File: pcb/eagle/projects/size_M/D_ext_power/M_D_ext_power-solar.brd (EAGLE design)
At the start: 30 parts

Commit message: changed type of 3.3V converter back to LM3671
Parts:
- D.L1: value 4u7 -> 2u2
- D.U2: value MCP1603T-330I -> LM3671_3.3
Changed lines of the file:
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@@
 <grid distance="1" unitdist="mil" unit="mil" style="lines" multiple="1" display="yes" altdistance="0.1" altunitdist="mm" altunit="mm"/>
 <layers>
-<layer number="1" name="Top" color="4" fill="1" visible="no" active="yes"/>
-<layer number="16" name="Bottom" color="1" fill="1" visible="no" active="yes"/>
+<layer number="1" name="Top" color="4" fill="1" visible="yes" active="yes"/>
+<layer number="16" name="Bottom" color="1" fill="1" visible="yes" active="yes"/>
 <layer number="17" name="Pads" color="2" fill="1" visible="yes" active="yes"/>
 <layer number="18" name="Vias" color="2" fill="1" visible="yes" active="yes"/>
@@
 <layer number="20" name="Dimension" color="24" fill="1" visible="yes" active="yes"/>
 <layer number="21" name="tPlace" color="23" fill="1" visible="yes" active="yes"/>
-<layer number="22" name="bPlace" color="47" fill="1" visible="no" active="yes"/>
+<layer number="22" name="bPlace" color="47" fill="1" visible="yes" active="yes"/>
 <layer number="23" name="tOrigins" color="15" fill="1" visible="yes" active="yes"/>
-<layer number="24" name="bOrigins" color="15" fill="1" visible="no" active="yes"/>
+<layer number="24" name="bOrigins" color="15" fill="1" visible="yes" active="yes"/>
 <layer number="25" name="tNames" color="7" fill="1" visible="yes" active="yes"/>
-<layer number="26" name="bNames" color="7" fill="1" visible="no" active="yes"/>
+<layer number="26" name="bNames" color="7" fill="1" visible="yes" active="yes"/>
 <layer number="27" name="tValues" color="7" fill="1" visible="no" active="yes"/>
 <layer number="28" name="bValues" color="7" fill="1" visible="no" active="yes"/>
-<layer number="29" name="tStop" color="7" fill="3" visible="yes" active="yes"/>
+<layer number="29" name="tStop" color="7" fill="3" visible="no" active="yes"/>
 <layer number="30" name="bStop" color="7" fill="6" visible="no" active="yes"/>
 <layer number="31" name="tCream" color="7" fill="4" visible="no" active="yes"/>
@@
 <layer number="37" name="tTest" color="7" fill="1" visible="no" active="yes"/>
 <layer number="38" name="bTest" color="7" fill="1" visible="no" active="yes"/>
-<layer number="39" name="tKeepout" color="4" fill="11" visible="no" active="yes"/>
-<layer number="40" name="bKeepout" color="1" fill="11" visible="no" active="yes"/>
-<layer number="41" name="tRestrict" color="4" fill="10" visible="no" active="yes"/>
-<layer number="42" name="bRestrict" color="1" fill="10" visible="no" active="yes"/>
+<layer number="39" name="tKeepout" color="4" fill="11" visible="yes" active="yes"/>
+<layer number="40" name="bKeepout" color="1" fill="11" visible="yes" active="yes"/>
+<layer number="41" name="tRestrict" color="4" fill="10" visible="yes" active="yes"/>
+<layer number="42" name="bRestrict" color="1" fill="10" visible="yes" active="yes"/>
 <layer number="43" name="vRestrict" color="2" fill="10" visible="no" active="yes"/>
 <layer number="44" name="Drills" color="7" fill="1" visible="no" active="yes"/>
@@
 <layer number="46" name="Milling" color="3" fill="1" visible="no" active="yes"/>
 <layer number="47" name="Measures" color="7" fill="1" visible="no" active="yes"/>
-<layer number="48" name="Document" color="49" fill="1" visible="yes" active="yes"/>
+<layer number="48" name="Document" color="49" fill="1" visible="no" active="yes"/>
 <layer number="49" name="Reference" color="7" fill="1" visible="no" active="yes"/>
 <layer number="50" name="dxf" color="7" fill="1" visible="no" active="no"/>
-<layer number="51" name="tDocu" color="7" fill="1" visible="no" active="yes"/>
-<layer number="52" name="bDocu" color="7" fill="1" visible="no" active="yes"/>
+<layer number="51" name="tDocu" color="7" fill="1" visible="yes" active="yes"/>
+<layer number="52" name="bDocu" color="7" fill="1" visible="yes" active="yes"/>
 <layer number="53" name="tGND_GNDA" color="7" fill="9" visible="no" active="no"/>
 <layer number="54" name="bGND_GNDA" color="1" fill="9" visible="no" active="no"/>
@@
 <attribute name="VALUE" x="9.68568125" y="17.89148125" size="0.8128" layer="27" rot="R180"/>
 </element>
-<element name="D.U2" library="!stavebnice03" package="SOT32-5" value="MCP1603T-330I" x="14.4145" y="12.99718125" smashed="yes" rot="MR0">
+<element name="D.U2" library="!stavebnice03" package="SOT32-5" value="LM3671_3.3" x="14.4145" y="12.99718125" smashed="yes" rot="MR0">
 <attribute name="NAME" x="15.765903125" y="12.643040625" size="0.8128" layer="26" rot="MR0"/>
 <attribute name="VALUE" x="16.8037" y="14.27558125" size="0.8128" layer="28" rot="MR270"/>
@@
 <attribute name="NAME" x="7.3928" y="2.863" size="0.8128" layer="26" ratio="15" rot="MR0"/>
 </element>
-<element name="D.L1" library="rcl" library_urn="urn:adsk.eagle:library:334" package="L3230M" package3d_urn="urn:adsk.eagle:package:23481/3" value="4u7" x="14.3002" y="16.4592" smashed="yes" rot="MR0">
+<element name="D.L1" library="rcl" library_urn="urn:adsk.eagle:library:334" package="L3230M" package3d_urn="urn:adsk.eagle:package:23481/3" value="2u2" x="14.3002" y="16.4592" smashed="yes" rot="MR0">
 <attribute name="NAME" x="14.711678125" y="17.650459375" size="0.8128" layer="26" rot="MR270"/>
 <attribute name="POPULARITY" value="0" x="14.3002" y="16.4592" size="1.778" layer="28" rot="MR0" display="off"/>

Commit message: minor changes for PCB v6.
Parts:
- added D.R11: 100k, rcl:R0603
- D.LIPOL: device pinhead2:1X02 -> pinhead2:1X02-2
- D.R10: value 10k? -> 0.1; device rcl:R0603 -> rcl:R0805
- D.R8: value 0.1 -> 10k?; device rcl:R0805 -> rcl:R0603
- moved D.T2 1.17 mm to (4.62, 6.76)
- moved D.R10 0.69 mm to (8.58, 13.9), flipped to the top, turned to 180 degrees
- moved D.R8 0.58 mm to (8.76, 14.6), flipped to the bottom, turned to 90 degrees
- moved D.C6 0.51 mm to (9.73, 16.5)
- moved D.R3 0.32 mm to (2.91, 16.2)
- moved D.LIPOL 0.26 mm to (4.95, 19.4)
- moved D.R9 0.26 mm to (6.22, 1.46)
- moved D.C7 0.13 mm to (9.79, 17.2)
- moved U$2 0.10 mm to (5.28, 13.8)
- moved D.R1 0.08 mm to (6.48, 5.99)
- moved D.R6 0.05 mm to (8.51, 9.17)
- moved D.T1 0.05 mm to (11.0, 11.6)
- moved U$1 0.05 mm to (14.4, 2.75)
- moved D.C2 0.05 mm to (17.8, 14.8)
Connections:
- net GND: now also D.R11.2
- net IN+: now also D.R10.2; no longer D.R8.2
- net IN-: now also D.R10.1; no longer D.R8.1
- net N$1: now also D.R11.1
- net N$8: now also D.R8.1; no longer D.R10.1
- net VUSB: now also D.R8.2; no longer D.R10.2
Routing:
- net GND: track 122.8 -> 125.8 mm, vias 4 -> 6
- net VCC: track 45.4 -> 42.4 mm
- net N$1: track 8.98 -> 10.9 mm
- net N$8: track 20.9 -> 22.5 mm
- net PA3: track 10.9 -> 9.78 mm
- net N$5: track 14.7 -> 13.8 mm
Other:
- board text added: "power solar M6"
- board text removed: "power M5"

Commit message: formal changes
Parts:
- D.R1: value 4k7 -> 5k1
- D.R7: value 390k -> 100k

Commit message: fet gates resistor increased to 390 k - lower power consumption
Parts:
- D.R11, D.R4, D.R7: value 100k -> 390k
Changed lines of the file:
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@@
 <attribute name="VALUE" x="7.874" y="11.076940625" size="1.27" layer="28" rot="MR180"/>
 </element>
-<element name="D.R7" library="rcl" library_urn="urn:adsk.eagle:library:334" package="R0603" package3d_urn="urn:adsk.eagle:package:23555/3" value="100k" x="14.47038125" y="9.9314" smashed="yes" rot="MR0">
+<element name="D.R7" library="rcl" library_urn="urn:adsk.eagle:library:334" package="R0603" package3d_urn="urn:adsk.eagle:package:23555/3" value="390k" x="14.47038125" y="9.9314" smashed="yes" rot="MR0">
 <attribute name="NAME" x="15.296159375" y="8.402340625" size="0.8128" layer="26" rot="MR0"/>
 <attribute name="POPULARITY" value="70" x="14.47038125" y="9.9314" size="1.778" layer="28" rot="MR0" display="off"/>
@@
 <attribute name="VALUE" x="1.4478" y="4.8514" size="1.27" layer="28" rot="MR90"/>
 </element>
-<element name="D.R4" library="rcl" library_urn="urn:adsk.eagle:library:334" package="R0603" package3d_urn="urn:adsk.eagle:package:23555/3" value="100k" x="10.3886" y="2.9718" smashed="yes" rot="R270">
+<element name="D.R4" library="rcl" library_urn="urn:adsk.eagle:library:334" package="R0603" package3d_urn="urn:adsk.eagle:package:23555/3" value="390k" x="10.3886" y="2.9718" smashed="yes" rot="R270">
 <attribute name="NAME" x="11.0236" y="1.143" size="0.8128" layer="25" rot="R180"/>
 <attribute name="POPULARITY" value="70" x="10.3886" y="2.9718" size="1.778" layer="27" rot="R270" display="off"/>
@@
 <attribute name="VALUE" x="6.858" y="13.9954" size="1.27" layer="28" rot="MR90"/>
 </element>
-<element name="D.R11" library="rcl" library_urn="urn:adsk.eagle:library:334" package="R0603" package3d_urn="urn:adsk.eagle:package:23555/3" value="100k" x="4.5974" y="9.1694" smashed="yes" rot="MR180">
+<element name="D.R11" library="rcl" library_urn="urn:adsk.eagle:library:334" package="R0603" package3d_urn="urn:adsk.eagle:package:23555/3" value="390k" x="4.5974" y="9.1694" smashed="yes" rot="MR180">
 <attribute name="NAME" x="5.4102" y="8.4836" size="0.7112" layer="26" rot="MR180"/>
 <attribute name="POPULARITY" value="70" x="4.5974" y="9.1694" size="1.778" layer="28" rot="MR180" display="off"/>

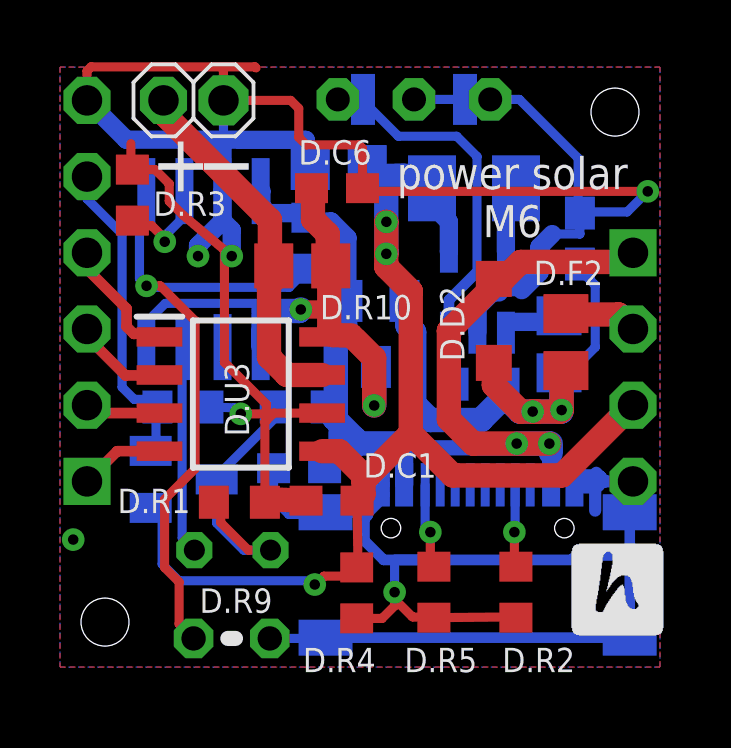
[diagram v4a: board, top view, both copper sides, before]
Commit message: usb moved to be possible to place in connected adapters
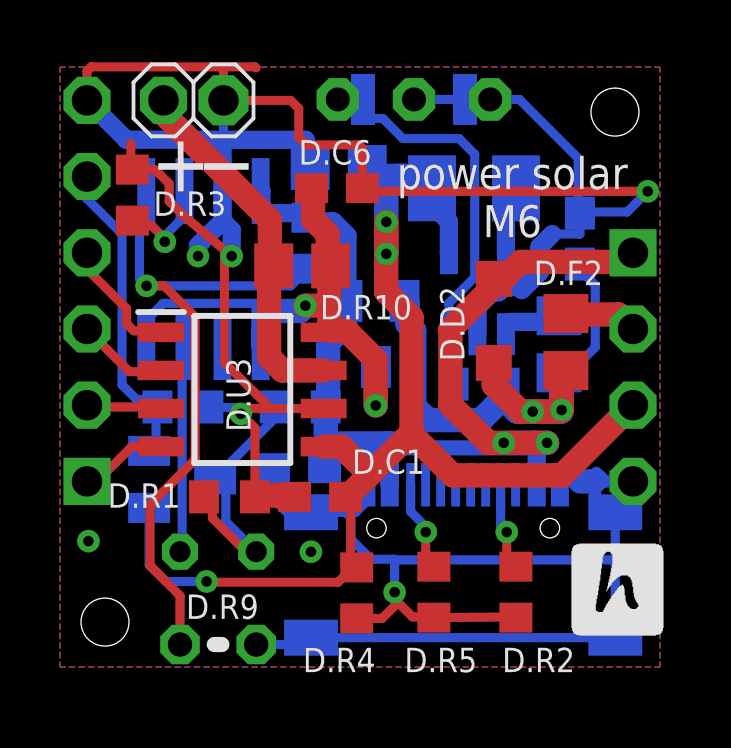
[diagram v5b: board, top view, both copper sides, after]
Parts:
- moved D.R9 0.50 mm to (5.77, 1.25)
- moved U$1 0.48 mm to (13.9, 2.75)
- moved D.D1 0.48 mm to (5.77, 3.95)
- moved D.C1 0.40 mm to (9.17, 6.17)
- moved D.R1 0.38 mm to (6.15, 6.17)
- moved D.U3 0.16 mm to (6.58, 9.75)
- moved D.U2 0.05 mm to (14.4, 12.9)
- moved D.T2 0.05 mm to (4.57, 6.76)
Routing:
- net VUSB: track 40.8 -> 37.9 mm
- net VCC: track 42.4 -> 43.7 mm
- net GND: track 125.8 -> 126.8 mm, vias 6 -> 7
- net PA3: track 9.78 -> 9.09 mm
- net IN-: track 21.6 -> 22.1 mm
